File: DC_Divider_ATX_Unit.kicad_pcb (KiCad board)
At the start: 2 copper layers, 53 x 60.5 mm, 5 parts, among them J1 ATX-24, J2 Conn_01x02, J3 Conn_01x02, J4 Conn_01x02, U1 YAAJ_DCDC_StepDown_LM2596

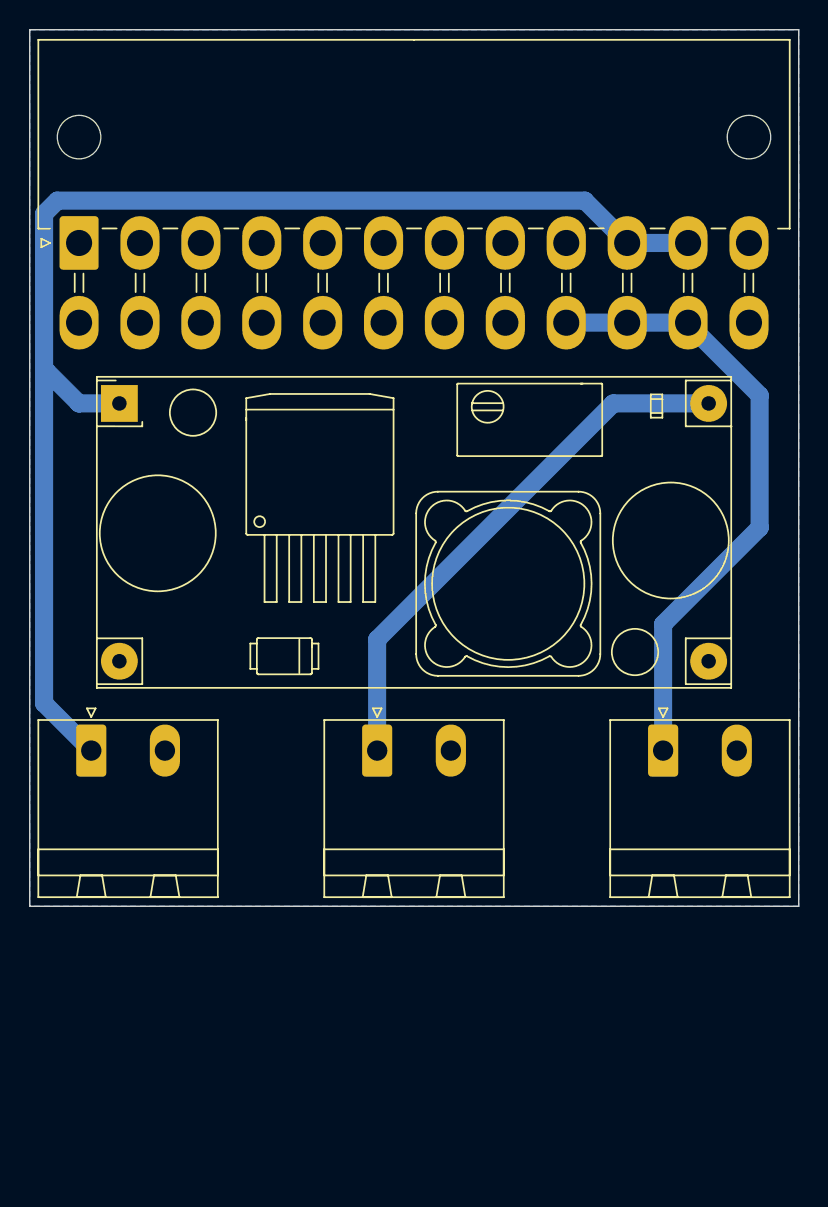
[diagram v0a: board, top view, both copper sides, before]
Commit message: Revised PCB design w/ space for fuse holders.
Minival-like blade fuse holders were included in series with each power rail in order to prevent catastrophic damage to the board in a short circuit/overcurrent situation.
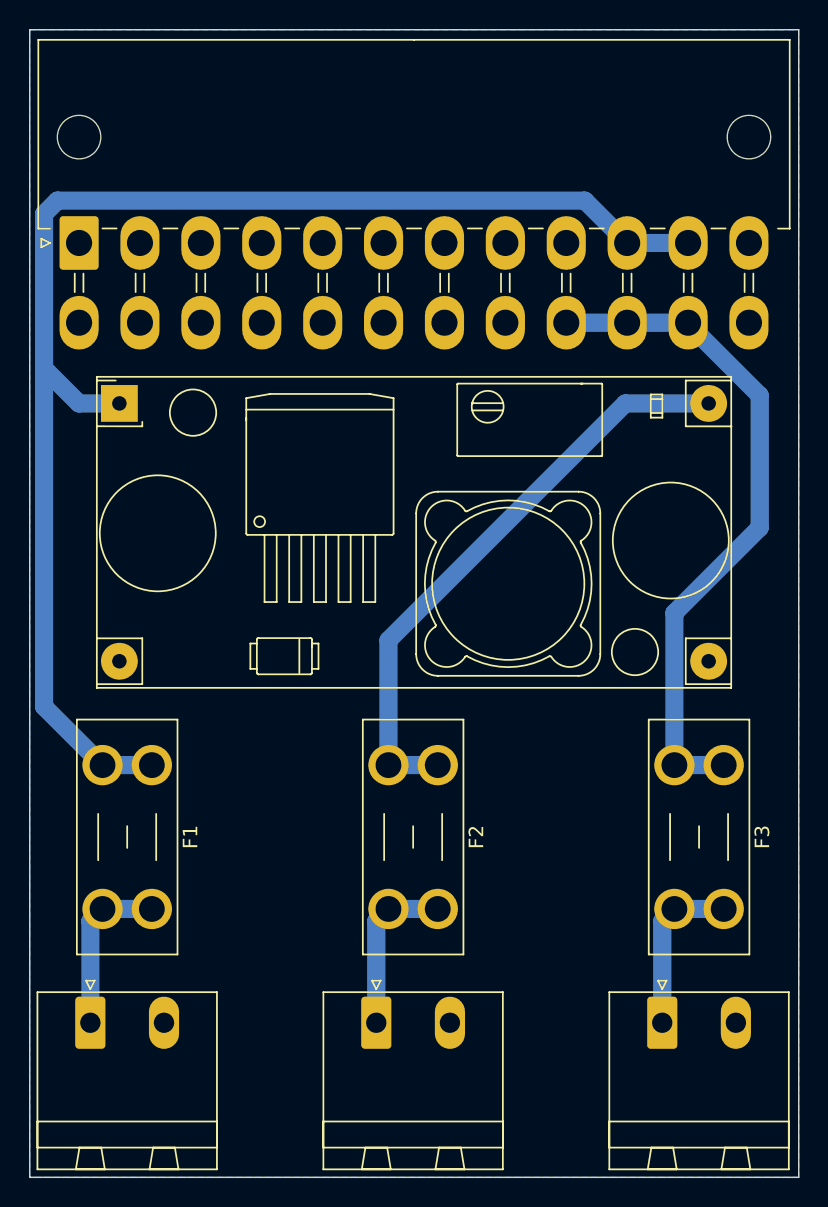
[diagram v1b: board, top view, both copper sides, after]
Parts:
- added F1: Fuse, Fuse:Fuseholder_Blade_Mini_Keystone_3568, F.Cu at (114.2, 135.0)
- added F2: Fuse, Fuse:Fuseholder_Blade_Mini_Keystone_3568, F.Cu at (133.9, 135.0)
- added F3: Fuse, Fuse:Fuseholder_Blade_Mini_Keystone_3568, F.Cu at (153.6, 135.0)
- moved J2 18.8 mm to (109.9, 152.8)
- moved J3 18.8 mm to (129.7, 152.8)
- moved J4 18.8 mm to (149.4, 152.8)
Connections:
- J2 pad 1: +12V -> Net-(J2-Pad1)
- J3 pad 1: +9V -> Net-(J3-Pad1)
- J4 pad 1: +5V -> Net-(J4-Pad1)
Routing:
- net Net-(J4-Pad1): track 0.00 -> 11.6 mm
- net Net-(J3-Pad1): track 0.00 -> 11.6 mm
- net Net-(J2-Pad1): track 0.00 -> 11.6 mm
- net +12V: track 90.5 -> 95.2 mm
- net +5V: track 42.7 -> 46.8 mm
- net +9V: track 37.3 -> 40.9 mm
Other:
- board size 53 x 60.5 mm -> 53 x 79.1 mm
